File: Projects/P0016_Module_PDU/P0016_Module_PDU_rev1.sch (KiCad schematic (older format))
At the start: 20 parts

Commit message: Moved out datasheets, made 1 footprint
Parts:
- removed J? (x6): 22-03-5045, symbol 22-03-5045
- removed J? (x2): 22-03-5035, symbol 22-03-5035
- removed U? (x4): LM1084ISX-ADJ/NOPB, symbol LM1084ISX-ADJ/NOPB
- added C? (x8): 10uF tantalum, symbol CP
- added C? (x2): 47pF, symbol C
- added C? (x2): 100uF, symbol CP1
- added C? (x2): 1uF, symbol C
- added IC?: ATTINY841-MU, QFN/MLF20, symbol ATTINY841-MU
- added J? (x6): 22-03-5045, symbol 22-03-5045
- added J? (x2): 22-03-5035, symbol 22-03-5035
- added J? (x2): 70543-0036, symbol 70543-0036
- added P?: USB_OTG, symbol USB_OTG
- added Q?: Q_PMOS_GSD, symbol Q_PMOS_GSD
- added R? (x5): 4k7, symbol R
- added R? (x9): 680, symbol R
- added R? (x6): 5k9, symbol R
- added R? (x2): 27, symbol R
- added R? (x2): 10k, symbol R
- added R?: 10K, symbol R
- added S?: GW12LCP, symbol GW12LCP
- added U?: SN65176BDR, symbol SN65176BDR
- added U? (x8): MIC29302AWU-TR, symbol MIC29302AWU-TR
- added U?: TC7W241FUTE12LF, symbol TC7W241FUTE12LF
- added U?: FT231XQ, symbol FT231XQ
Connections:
- net labels added: 5V, RS485+, RS485-, RX_USB, TTL_BUS, TXDEN_USB, TX_USB
- wire segments 28 -> 326
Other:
- note added: "0.005ohm"
- note added: "0.20 V/A"
- note added: "DMP2035U-7"
- note added: "Interlock 1"
- note added: "Interlock 2"
- note added: "On"
- moved on the sheet: C?, J?, R?, U?

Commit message: More work on PDU schematic
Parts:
- added C? (x2): 100uF, symbol CP1
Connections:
- wire segments 326 -> 241

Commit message: updated project 8
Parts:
- removed IC?: ATTINY841-MU, QFN/MLF20, symbol ATTINY841-MU
- removed R?: 680, symbol R
- removed R? (x2): 4k7, symbol R
- added IC?: ATMEGA328P-A, TQFP32, symbol ATMEGA328P-A
- added L?: 10uH, symbol L_Small
- added Q?: BSS138, SOT-23, symbol BSS138
- added R?: 40k, symbol R
- added R?: 10k, symbol R
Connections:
- net labels added: EN1, EN2, EN3, EN4, EN5, EN6, EN7, EN8, RX_uC, TXDEN_uC, TX_uC, VIN, VSENSE
- wire segments 241 -> 319
- no-connect marks 0 -> 3
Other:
- note added: "V_SENSE 0.20 V/V"
- moved on the sheet: C?, P?, R?, U?

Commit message: revised P0008, added gerbers
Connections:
- wire segments 319 -> 318
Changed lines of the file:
@@
 Data
 89 50 4E 47 0D 0A 1A 0A 00 00 00 0D 49 48 44 52 00 00 00 84 00 00 00 84 08 03 00 00 00 66 9A 73
-95 00 00 00 03 73 42 49 54 08 08 08 DB E1 4F E0 00 00 01 71 50 4C 54 45 01 00 00 5B 5B 5C 2B 2B
+95 00 00 00 03 73 42 49 54 08 08 08 DB E1 4F E0 00 00 01 71 50 4C 54 45 02 00 00 5B 5B 5C 2B 2B
 2B 22 07 09 34 0A 0E 3A 0B 0F 29 25 25 2B 09 0C 24 0B 0D 34 34 34 68 67 68 3A 3A 3B 4C 0D 13 6B
 12 1B 9C 1A 26 B4 1D 2C BF 1E 2E 7F 16 20 63 64 64 AB 1C 2A 8E 18 23 64 11 19 3E 0B 10 1E 13 14
@@
 1C 3E 3F 40 4E 51 53 6F 6F 70 80 7F 80 0F 10 10 2E 2F 30 0F 0F 10 57 5A 5C E0 DF E0 46 4A 4C 17
 18 18 5C 5E 60 B7 B8 B9 BE BE C0 1F 1F 20 8F 8F 90 1D 0B 0C 27 28 29 1E 0F 10 46 47 48 26 1F 20
-2F 30 31 37 38 39 75 73 74 DC 64 69 7C 00 00 00 01 74 52 4E 53 00 40 E6 D8 66 00 00 15 0B 49 44
+2F 30 31 37 38 39 75 73 74 78 36 5E 62 00 00 00 01 74 52 4E 53 00 40 E6 D8 66 00 00 15 0B 49 44
 41 54 78 9C BD 5C 89 43 DA CA D6 57 5C 30 B2 16 C4 85 BA 57 45 6D 4B AD 20 54 33 2C B5 22 8B 95
 0C 52 54 52 4B 31 54 11 2B B6 F4 F5 76 F9 FE FA EF CC 4C 42 16 02 F6 F2 EE 7D A7 6A 60 92 CC F9
@@
 AA 3A 6B 5E F4 95 4C FE 1D FA A9 32 D3 19 7D E8 45 BB BD 3F FF FC B7 88 B3 FA 26 A8 E8 67 96 74
 ED F2 03 04 D7 8C BD EF F7 21 FF 16 CD 72 7F D9 E7 1D 06 27 B8 66 9F 98 F0 8D 4C 71 83 E6 F7 FC
-AF 68 BC EF FF 0B E4 FF 01 8C 6E BB 14 85 49 1E 74 00 00 00 00 49 45 4E 44 AE 42 60 82 E0
+AF 68 BC EF FF 0B E4 FF 01 8C 6E BB 14 85 49 1E 74 00 00 00 00 49 45 4E 44 AE 42 60 82 00
 EndData
 $EndBitmap
@@
 	6450 5800 6700 5800
 Wire Wire Line
-	10450 6450 10450 6450
-Wire Wire Line
 	2200 1800 2500 1800

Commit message: Simplifying PDU
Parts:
- removed C? (x2): 10uF tantalum, symbol CP
- removed C?: 100uF, symbol CP1
- removed C?: 1uF, symbol C
- removed J? (x2): 22-03-5035, symbol 22-03-5035
- removed R? (x2): 4k7, symbol R
- removed R? (x2): 680, symbol R
- removed R?: 10K, symbol R
- removed U? (x2): MIC29302AWU-TR, symbol MIC29302AWU-TR
- removed U?: TC7W241FUTE12LF, symbol TC7W241FUTE12LF
- added C? (x2): 47pF, symbol C
- added C? (x2): 1uF, symbol C
- added C? (x2): 18pF, symbol C
- added C?: 100nF, symbol C
- added D? (x4): LTST-C170KFKT, symbol LTST-C170KFKT
- added P?: USB_OTG, symbol USB_OTG
- added R? (x2): 27, symbol R
- added R? (x2): 10k, symbol R
- added R?: 1k, symbol R
- added RP?: R_PACK4, symbol R_PACK4
- added U?: FT231XQ, symbol FT231XQ
- added U?: SN65176BDR, symbol SN65176BDR
- added Y?: ABM8-16.000MHZ-10-1-U-T, symbol ABM8-16.000MHZ-10-1-U-T
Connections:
- net labels added: RX_PGM, TX_PGM, XTAL1, XTAL2, ~ARD_PGM, ~RST, ~RX_LED_PGM, ~RX_LED_USB, ~TX_LED_PGM, ~TX_LED_USB
- net labels removed: EN7, EN8, TTL_BUS
- wire segments 318 -> 243
- no-connect marks 3 -> 6
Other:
- moved on the sheet: C?, IC?, J?, L?, Q?, R?, U?

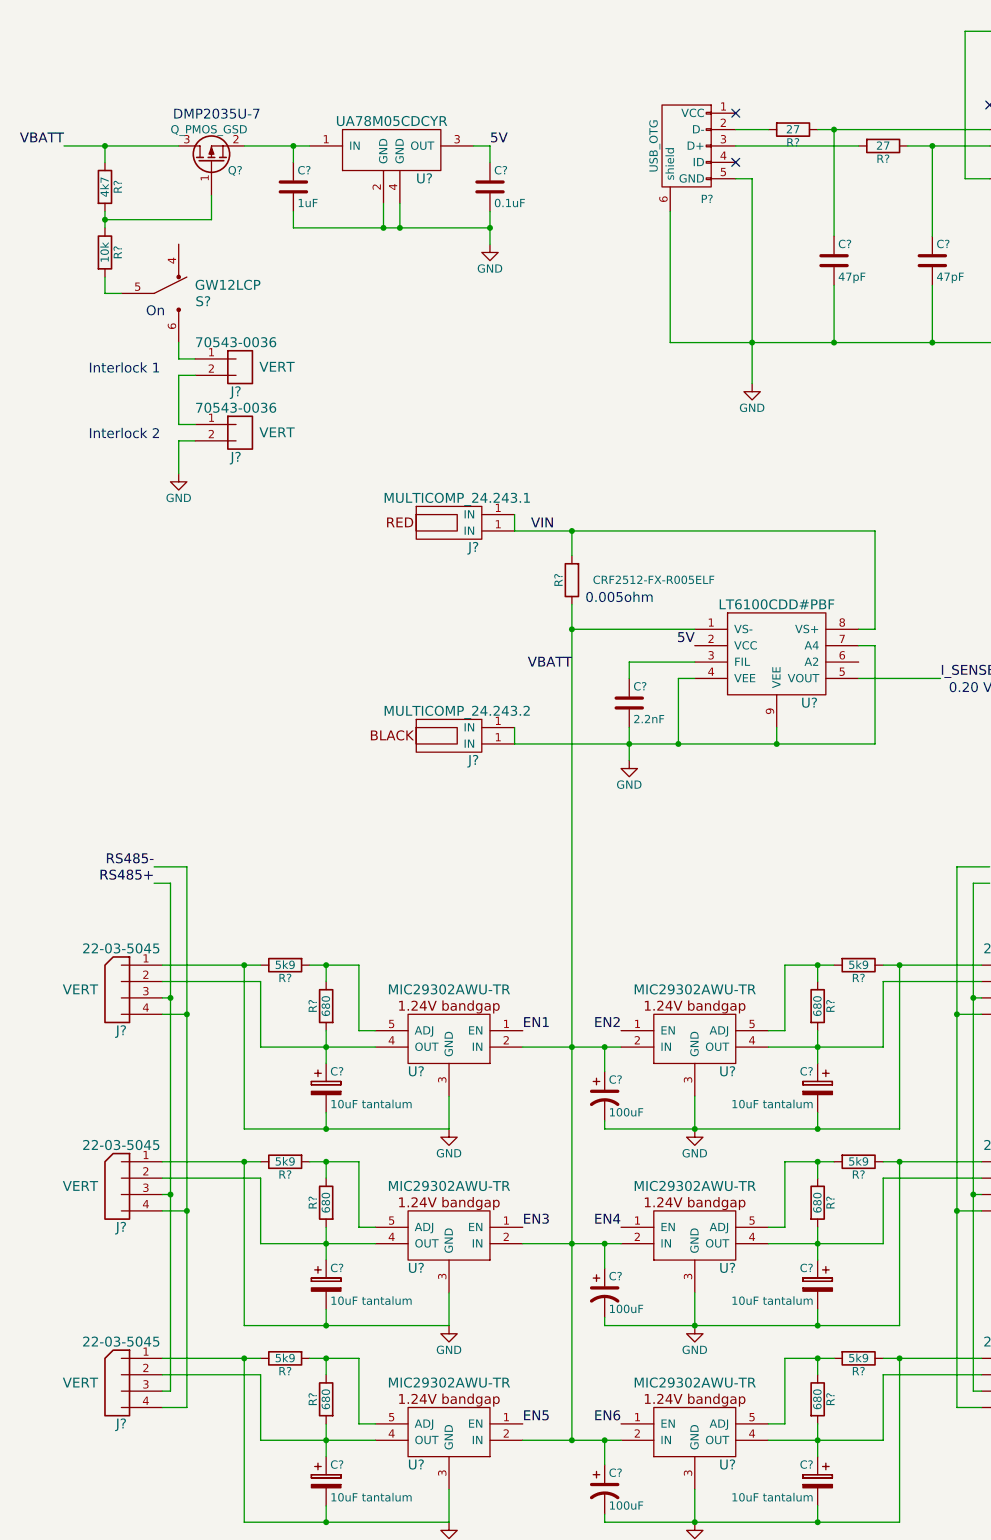
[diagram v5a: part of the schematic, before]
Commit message: Simplified power on switch
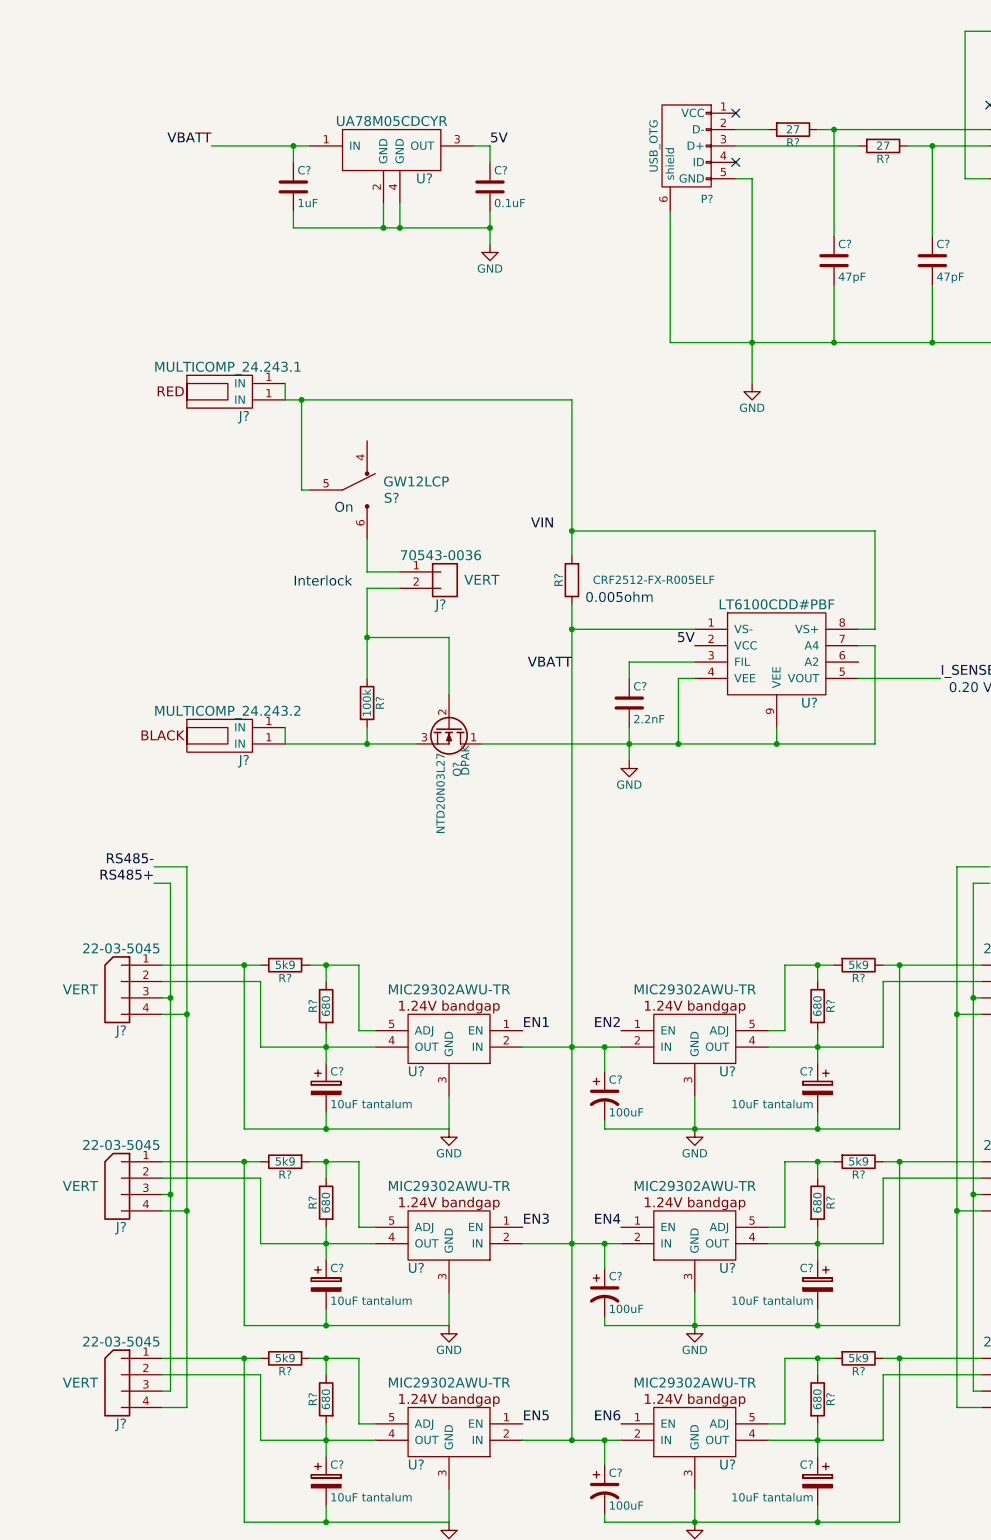
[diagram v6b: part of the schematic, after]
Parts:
- removed J?: 70543-0036, symbol 70543-0036
- removed Q?: Q_PMOS_GSD, symbol Q_PMOS_GSD
- removed R?: 4k7, symbol R
- removed R?: 10k, symbol R
- added Q?: NTD20N03L27, DPAK, symbol Q_NMOS_DGS
- added R?: 100k, symbol R
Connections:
- net GND: now also Q?.1 (D); no longer J?.1 (IN)
- net VBATT: now also C?.1, U?.1 (IN)
- net VIN: no longer J?.1 (IN), R?.2, U?.8 (VS+)
- net at J?.2: now also Q?.2 (G), R?.1
- net at S?.5: now also J?.1 (IN), R?.2, U?.8 (VS+)
- new net: J?.1 (IN), Q?.3 (S), R?.2
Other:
- note added: "Interlock"
- note removed: "DMP2035U-7"
- note removed: "Interlock 1"
- note removed: "Interlock 2"
- moved on the sheet: J?, S?

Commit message: Started layout for PDU module
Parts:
- removed Q?: BSS138, SOT-23, symbol BSS138
- removed RP?: R_PACK4, symbol R_PACK4
- added D1, D10, D11, D3, D5, D7, D9: LTST-C170KGKT, LEDs:LED_0805, symbol LTST-C170KGKT
- added D12: LTST-C170KRKT, LEDs:LED_0805, symbol LTST-C170KRKT
- added J6: 70543-0036, Pin_Headers:Pin_Header_Straight_1x02, symbol 70543-0036
- added P3: ICSP_02X03, Pin_Headers:Pin_Header_Straight_2x03, symbol ICSP_02X03
- added R25, R26, R27, R28, R29, R30, R31, R32, R33, R34, R35, R36: 680, Resistors_SMD:R_0603, symbol R
- C1, C10, C11, C12, C2, C3, C6, C7, C8: renamed from C?; footprint (none) -> Capacitors_SMD:c_elec_5x4.5
- C13, C14, C15, C16, C17, C18, C19, C20, C21, C22, C4, C5, C9: renamed from C?; footprint (none) -> Capacitors_SMD:C_0805
- D2, D4, D6, D8: renamed from D?; footprint (none) -> LEDs:LED_0805
- IC1: renamed from IC?; footprint TQFP32 -> Housings_QFP:TQFP-32_7x7mm_Pitch0.8mm
- J1, J10, J2, J3, J8, J9: renamed from J?; footprint (none) -> Pin_Headers:Pin_Header_Straight_1x04
- J4, J5: renamed from J?; footprint (none) -> open_robotics:MULTICOMP_4MM_JACK
- J7: renamed from J?; footprint (none) -> Pin_Headers:Pin_Header_Straight_1x02
- L1: renamed from L?; footprint (none) -> Capacitors_SMD:C_0603
- P1, P2: renamed from P?; footprint (none) -> Connect:USB_Micro-B_10103594-0001LF
- Q1: renamed from Q?; footprint DPAK -> TO_SOT_Packages_SMD:TO-252-2Lead
- R1, R10, R11, R12, R13, R14, R15, R16, R17, R18, R19, R2, R20, R21, R22, R23, R24, R3, R4, R5, R6, R7, R9: renamed from R?; footprint (none) -> Resistors_SMD:R_0603
- R8: renamed from R?; footprint (none) -> Resistors_SMD:R_2512
- S1: renamed from S?; footprint (none) -> open_robotics:GW12LCP_SWITCH_SPDT
- U1, U2, U3, U5, U6, U7: renamed from U?; footprint (none) -> TO_SOT_Packages_SMD:TO-263-5Lead
- U10, U11: renamed from U?; footprint (none) -> Housings_SOIC:SOIC-8_3.9x4.9mm_Pitch1.27mm
- U12, U9: renamed from U?; footprint (none) -> Housings_DFN_QFN:QFN-20-1EP_4x4mm_Pitch0.5mm
- U4: renamed from U?; footprint (none) -> TO_SOT_Packages_SMD:SOT-223
- U8: renamed from U?; footprint (none) -> Housings_DFN_QFN:DFN-8-1EP_3x3mm_Pitch0.5mm
- Y1: renamed from Y?; footprint (none) -> open_robotics:CSMD-ABM8
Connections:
- net 5V: now also P3.2 (VTG), R26.1, R28.1, R30.1, R31.1, R35.1
- net EN1: now also R25.1
- net EN2: now also R27.1
- net EN3: now also R29.1
- net EN4: now also R32.1
- net EN5: now also R33.1
- net EN6: now also R34.1
- net GND: now also D1.1 (K), D10.1 (K), D11.1 (K), D12.1 (K), D3.1 (K), D5.1 (K), D7.1 (K), D9.1 (K), P3.6 (GND)
- net TXDEN_uC: now also IC1.14 ((PCINT2/OC1B/~SS~)PB2); no longer IC1.17 ((PCINT5/SCK)PB5)
- net VBATT: now also R21.1
- net VIN: now also J4.1 (IN), R8.2, S1.5, U8.8 (VS+); no longer R21.1
- net VSENSE: now also R21.2
- net ~RST: now also P3.5 (~RST)
- net at J7.1, S1.6: now also J6.1
- net at J7.2, Q1.2 (G), R7.1: now also J6.2
- net ERR: now reaches IC1.12 ((PCINT0/CLKO/ICP1)PB0)
- net ERR: now also R36.1
- net MOSI: now reaches IC1.15 ((PCINT3/OC2A/MOSI)PB3)
- net MOSI: now also P3.4 (MOSI)
- net MISO: now reaches IC1.16 ((PCINT4/MISO)PB4)
- net MISO: now also P3.1 (MISO)
- net at D2.2 (A): now also R26.2
- net at D4.2 (A): now also R28.2
- net at D6.2 (A): now also R30.2
- net at D8.2 (A): now also R31.2
- new net: D1.2 (A), R25.2
- new net: D3.2 (A), R27.2
- new net: D5.2 (A), R29.2
- new net: D7.2 (A), R32.2
- new net: D9.2 (A), R33.2
- new net: D10.2 (A), R34.2
- new net: D11.2 (A), R35.2
- new net: D12.2 (A), R36.2
- new net SCK: IC1.17 ((PCINT5/SCK)PB5), P3.3 (SCK)
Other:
- note added: "V_SENSE \n0.20 V/V"
- note removed: "V_SENSE 0.20 V/V"
- moved on the sheet: C13, C14, C15, C16, C17, C18, C19, C20, C21, C22, C4, C5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

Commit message: Created RS485 to TTL adapter
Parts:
- added C23, C24: 0.1uF, Capacitors_SMD:C_0805, symbol C
- added P10, P20: CONN_01X08, Pin_Headers:Pin_Header_Straight_1x08, symbol CONN_01X08
- added P11, P12, P13, P14, P16, P17, P18, P19: CONN_02X08, Pin_Headers:Pin_Header_Straight_2x08, symbol CONN_02X08
- added P15: CONN_01X16, Pin_Headers:Pin_Header_Straight_1x16, symbol CONN_01X16
- added P21, P22: CONN_01X01, Pin_Headers:Pin_Header_Straight_1x01, symbol CONN_01X01
- added P23: CONN_01X02, Pin_Headers:Pin_Header_Straight_1x02, symbol CONN_01X02
- added P4, P5, P6, P7, P8, P9: CONN_01X03, Pin_Headers:Pin_Header_Straight_1x03, symbol CONN_01X03
- added U13, U14: NCP1117ST50T3GOSCT, TO_SOT_Packages_SMD:SOT-223, symbol NCP1117ST50T3GOSCT
- added X1, X2, X3, X4, X5, X6: OP_HOLE, open_robotics:modular8_mounting_hole, symbol OP_HOLE
- renumbered J7 to J10, J8 to J2, J2 to J3, J9 to J4, J3 to J5, J10 to J6, J4 to J7, J5 to J8, J6 to J9
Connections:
- net EN1: now also IC1.26 ((PCINT11/ADC3)PC3); no longer IC1.32 ((PCINT18/INT0)PD2)
- net EN2: now also IC1.32 ((PCINT18/INT0)PD2); no longer IC1.1 ((PCINT19/OC2B/INT1)PD3)
- net EN4: now also IC1.23 ((PCINT8/ADC0)PC0); no longer IC1.9 ((PCINT21/OC0B/T1)PD5)
- net EN5: now also IC1.24 ((PCINT9/ADC1)PC1); no longer IC1.10 ((PCINT22/OC0A/AIN0)PD6)
- net EN6: now also IC1.25 ((PCINT10/ADC2)PC2); no longer IC1.11 ((PCINT23/AIN1)PD7)
- net GND: now also C23.2, C24.2, P15.1 (P1), P15.10 (P10), P15.11 (P11), P15.12 (P12), P15.13 (P13), P15.14 (P14), P15.15 (P15), P15.16 (P16), P15.2 (P2), P15.3 (P3), P15.4 (P4), P15.5 (P5), P15.6 (P6), P15.7 (P7), P15.8 (P8), P15.9 (P9), P4.1 (P1), P5.1 (P1), P6.1 (P1), P7.1 (P1), P8.1 (P1), P9.1 (P1), U13.1 (GND), U14.1 (GND)
- net TXDEN_uC: now also IC1.11 ((PCINT23/AIN1)PD7); no longer IC1.14 ((PCINT2/OC1B/~SS~)PB2)
- net V3_12V: now reaches C2.1, J3.2, R5.2, U2.4 (OUT)
- net V3_12V: now also P21.1 (P1), U14.3 (IN)
- net V4_12V: now reaches C11.1, J4.2, R10.2, U6.4 (OUT)
- net V4_12V: now also P22.1 (P1), U13.3 (IN)
- net 9/PB1/OC1A: now reaches IC1.13 ((PCINT1/OC1A)PB1)
- net 9/PB1/OC1A: now also P5.3 (P3)
- net SDA: now reaches IC1.27 ((PCINT12/SDA/ADC4)PC4)
- net SDA: now also P23.1 (P1)
- net SCL: now reaches IC1.28 ((PCINT13/SCL/ADC5)PC5)
- net SCL: now also P23.2 (P2)
- net MOSI renamed 11/PB3/OC2A
- net 11/PB3/OC2A: now also P6.3 (P3)
- new net 10/PB2/OC1B: IC1.14 ((PCINT2/OC1B/~SS~)PB2), P8.3 (P3)
- new net 3/PD3/OC2B: IC1.1 ((PCINT19/OC2B/INT1)PD3), P9.3 (P3)
- new net 5/PD5/OC0B: IC1.9 ((PCINT21/OC0B/T1)PD5), P7.3 (P3)
- new net 5V_POW_LEFT: C24.1, P10.1 (P1), P10.2 (P2), P10.3 (P3), P10.4 (P4), P10.5 (P5), P10.6 (P6), P10.7 (P7), P10.8 (P8), P4.2 (P2), P5.2 (P2), P6.2 (P2), U14.2 (OUT), U14.4 (OUT)
- new net 5V_POW_RIGHT: C23.1, P20.1 (P1), P20.2 (P2), P20.3 (P3), P20.4 (P4), P20.5 (P5), P20.6 (P6), P20.7 (P7), P20.8 (P8), P7.2 (P2), P8.2 (P2), P9.2 (P2), U13.2 (OUT), U13.4 (OUT)
- new net 6/PD6/OC0A: IC1.10 ((PCINT22/OC0A/AIN0)PD6), P4.3 (P3)
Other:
- note added: "External USB serial to RS485 bus"
- note added: "Microcontroller onto RS485 bus"
- note added: "Microcontroller programmer communication"
- note added: "Mounting holes\nCorners of board and by power-in"
- note added: "RS485 bus communication"
- moved on the sheet: C1, C10, C11, C12, C13, C14, C15, C17, C19, C2, C20, C21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
